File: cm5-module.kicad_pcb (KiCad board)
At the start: 4 copper layers, 100 x 100 mm, 156 parts, among them J1 DIN-41612-connector_090319679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, J10 MicroSD_5033981892, J2 CM5_1-100_3mm-stack, J3 CM5_101-200_3mm-stack, J4 JST_SH_1x3_BM03B-SRSS-TB-LF-SN, J5 Bus_M.2_1-2199230-6, J6 RJ45_HC612601A-M893-A, J7 USB-A_USB-303WSD-BRY, J8 HDMI-A_HDMI-19PIN-043, J9 USB-C_USB-310F-B-SU, Q1 SIS472DN-T1-GE3, Q2 SIS472DN-T1-GE3, Q3 AO3400A, U1 AP22615AWU-7, U10 AP22615AWU-7, U11 AP22615AWU-7, U2 AP22615AWU-7, U3 FT230XQ-R, U4 NTS0102DP, U5 CH334P, U6 LM74700QDBVRQ1, U7 SIC431AED-T1-GE3, U8 LM74700QDBVRQ1, U9 TPS564247DRLR, Y1 Oscillator_32.768kHz_OK2EL89C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, Y2 X322512MSB4SI

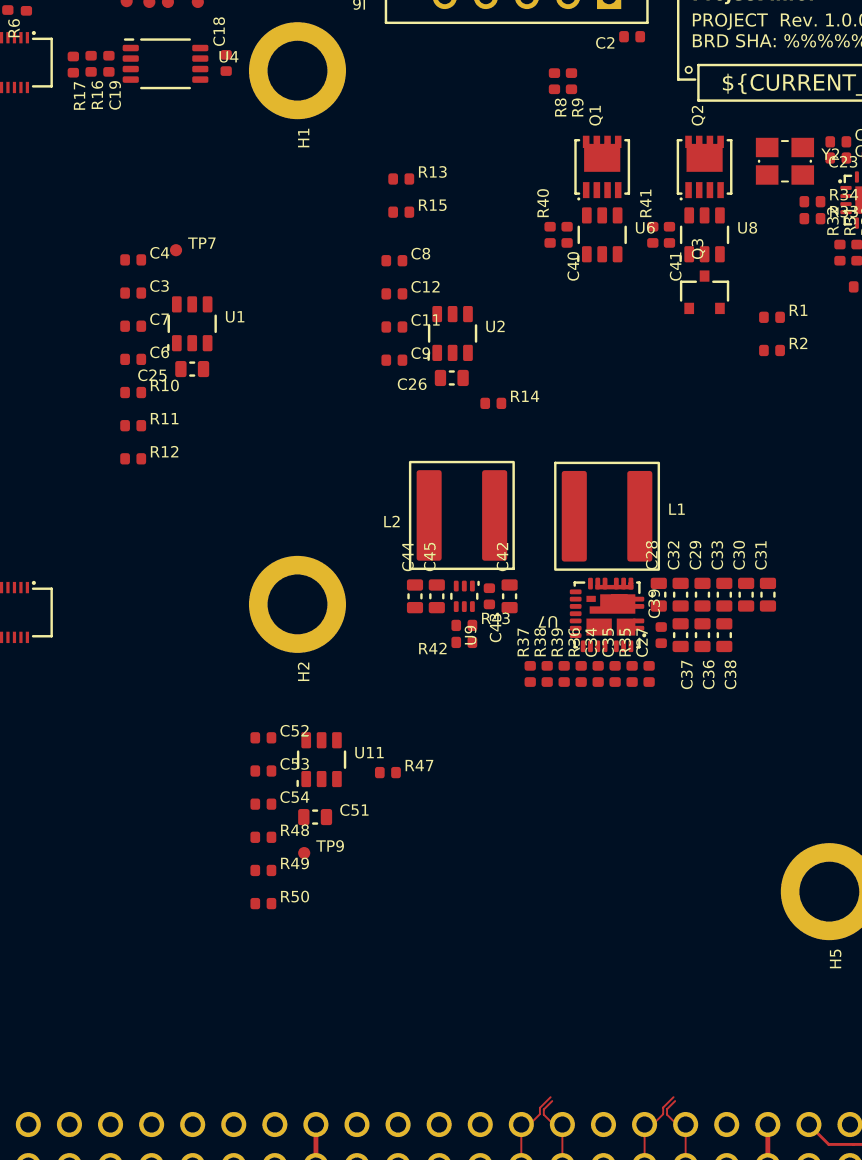
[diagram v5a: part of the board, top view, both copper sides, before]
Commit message: [#1] Finish schematic design of the 3V3 DC-DC converter
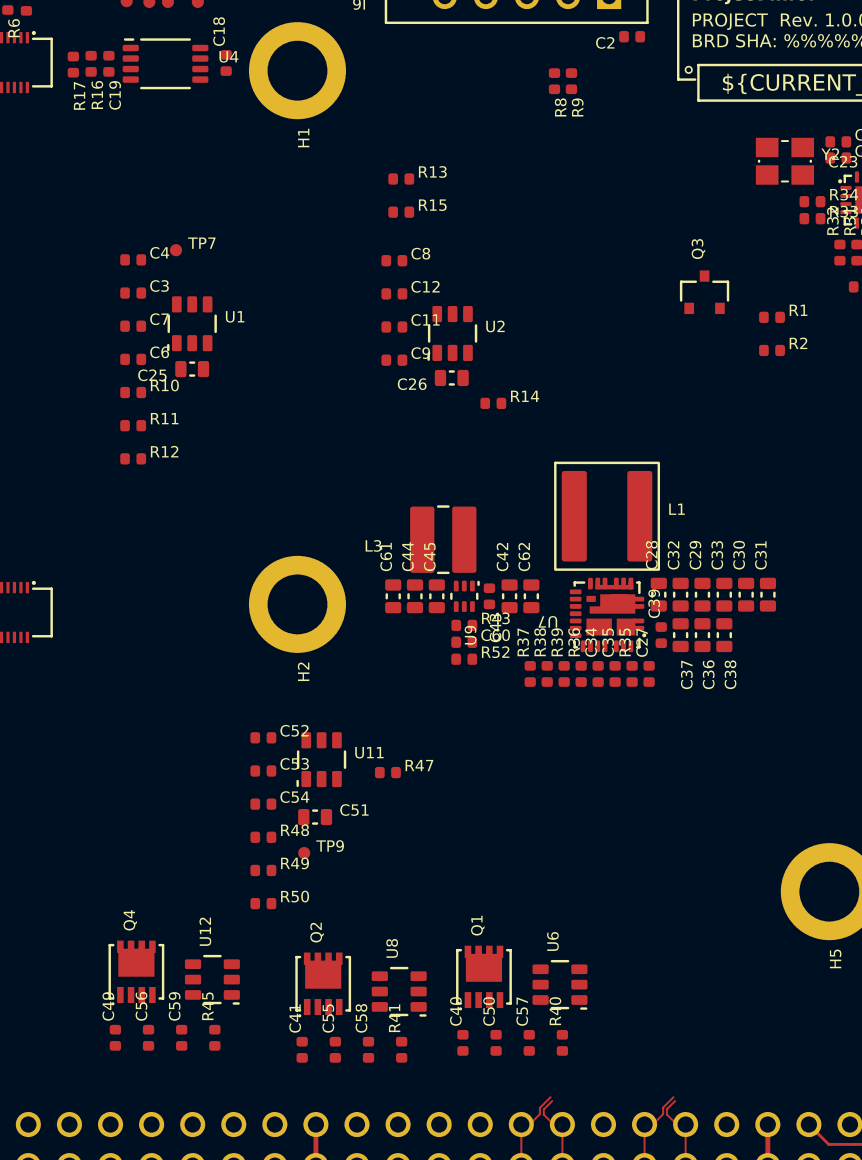
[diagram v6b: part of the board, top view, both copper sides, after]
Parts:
- removed L2: L-1u-20A-CJiang-FEXL0650A, DW-footprints:L-CJiang-FEXL0650A
- removed R42: R-10k-0402, DW-footprints:R_0402_1005Metric
- added C49: C-100n-0402, DW-footprints:C_0402_1005Metric, F.Cu at (83.3, 135.5)
- added C50: C-100n-0402, DW-footprints:C_0402_1005Metric, F.Cu at (106.9, 135.8)
- added C55: C-100n-0402, DW-footprints:C_0402_1005Metric, F.Cu at (96.9, 136.3)
- added C56: C-100n-0402, DW-footprints:C_0402_1005Metric, F.Cu at (85.4, 135.5)
- added C57: C-100n-0402, DW-footprints:C_0402_1005Metric, F.Cu at (108.9, 135.8)
- added C58: C-100n-0402, DW-footprints:C_0402_1005Metric, F.Cu at (99.0, 136.3)
- added C59: C-100n-0402, DW-footprints:C_0402_1005Metric, F.Cu at (87.4, 135.5)
- added C60: C-47p-0402, DW-footprints:C_0402_1005Metric, F.Cu at (104.9, 111.1)
- added C61: C-10u-0603, DW-footprints:C_0603_1608Metric, F.Cu at (100.5, 108.2)
- added C62: C-10u-0603, DW-footprints:C_0603_1608Metric, F.Cu at (109.0, 108.2)
- added L3: L-1u5-6.5A-CJiang-FTC404030S, DW-footprints:L-CJiang-FTC404030S, F.Cu at (103.6, 104.7)
- added Q4: SIS472DN-T1-GE3, DW-footprints:PowerPAK-1212-8_Single, F.Cu at (84.6, 131.5)
- added R45: R-10k-0402, DW-footprints:R_0402_1005Metric, F.Cu at (89.5, 135.5)
- added R52: R-45k3-0402, DW-footprints:R_0402_1005Metric, F.Cu at (104.9, 112.1)
- added U12: LM74700QDBVRQ1, DW-footprints:SOT-23-6, F.Cu at (89.3, 131.9)
- moved Q2 55.7 mm to (96.2, 132.2)
- moved C41 55.3 mm to (94.9, 136.3), turned to 90 degrees
- moved R41 52.7 mm to (101.0, 136.3)
- moved Q1 50.6 mm to (106.1, 131.8)
- moved U8 50.5 mm to (100.9, 132.7), turned to 90 degrees
- moved C40 50.4 mm to (104.8, 135.8), turned to 90 degrees
- moved R40 50.0 mm to (111.0, 135.8)
- moved U6 46.4 mm to (110.8, 132.2), turned to 90 degrees
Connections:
- net /Backplane/GPIOC0 renamed /Backplane/GPIO_C0
- net /Backplane/GPIOC1 renamed /Backplane/GPIO_C1
- net /Backplane/GPIOC10 renamed /Backplane/GPIO_C10
- net /Backplane/GPIOC11 renamed /Backplane/GPIO_C11
- net /Backplane/GPIOC12 renamed /Backplane/GPIO_C12
- net /Backplane/GPIOC13 renamed /Backplane/GPIO_C13
- net /Backplane/GPIOC14 renamed /Backplane/GPIO_C14
- net /Backplane/GPIOC15 renamed /Backplane/GPIO_C15
- net /Backplane/GPIOC2 renamed /Backplane/GPIO_C2
- net /Backplane/GPIOC3 renamed /Backplane/GPIO_C3
- net /Backplane/GPIOC4 renamed /Backplane/GPIO_C4
- net /Backplane/GPIOC5 renamed /Backplane/GPIO_C5
- net /Backplane/GPIOC6 renamed /Backplane/GPIO_C6
- net /Backplane/GPIOC7 renamed /Backplane/GPIO_C7
- net /Backplane/GPIOC8 renamed /Backplane/GPIO_C8
- net /Backplane/GPIOC9 renamed /Backplane/GPIO_C9
- net /Backplane/GPIOL0 renamed /Backplane/GPIO_L0
- net /Backplane/GPIOL1 renamed /Backplane/GPIO_L1
- net /Backplane/GPIOL10 renamed /Backplane/GPIO_L10
- net /Backplane/GPIOL11 renamed /Backplane/GPIO_L11
- net /Backplane/GPIOL12 renamed /Backplane/GPIO_L12
- net /Backplane/GPIOL13 renamed /Backplane/GPIO_L13
- net /Backplane/GPIOL14 renamed /Backplane/GPIO_L14
- net /Backplane/GPIOL15 renamed /Backplane/GPIO_L15
- net /Backplane/GPIOL2 renamed /Backplane/GPIO_L2
- net /Backplane/GPIOL3 renamed /Backplane/GPIO_L3
- net /Backplane/GPIOL4 renamed /Backplane/GPIO_L4
- net /Backplane/GPIOL5 renamed /Backplane/GPIO_L5
- net /Backplane/GPIOL6 renamed /Backplane/GPIO_L6
- net /Backplane/GPIOL7 renamed /Backplane/GPIO_L7
- net /Backplane/GPIOL8 renamed /Backplane/GPIO_L8
- net /Backplane/GPIOL9 renamed /Backplane/GPIO_L9
- net /Backplane/GPIOR0 renamed /Backplane/GPIO_R0
- net /Backplane/GPIOR1 renamed /Backplane/GPIO_R1
- net /Backplane/GPIOR10 renamed /Backplane/GPIO_R10
- net /Backplane/GPIOR11 renamed /Backplane/GPIO_R11
- net /Backplane/GPIOR12 renamed /Backplane/GPIO_R12
- net /Backplane/GPIOR13 renamed /Backplane/GPIO_R13
- net /Backplane/GPIOR14 renamed /Backplane/GPIO_R14
- net /Backplane/GPIOR15 renamed /Backplane/GPIO_R15
- net /Backplane/GPIOR2 renamed /Backplane/GPIO_R2
- net /Backplane/GPIOR3 renamed /Backplane/GPIO_R3
- net /Backplane/GPIOR4 renamed /Backplane/GPIO_R4
- net /Backplane/GPIOR5 renamed /Backplane/GPIO_R5
- net /Backplane/GPIOR6 renamed /Backplane/GPIO_R6
- net /Backplane/GPIOR7 renamed /Backplane/GPIO_R7
- net /Backplane/GPIOR8 renamed /Backplane/GPIO_R8
- net /Backplane/GPIOR9 renamed /Backplane/GPIO_R9
- net /USB hub/USB_1.D+ renamed /CAN to USB/USB.D+
- net /USB hub/USB_1.D- renamed /CAN to USB/USB.D-
- net /USB hub/USB_2.D+ renamed /CAN to USB1/USB.D+
- net /USB hub/USB_2.D- renamed /CAN to USB1/USB.D-
- net Net-(U6-EN) renamed /Power/Ideal diode 0/~{DISABLE}
- C15 pad 2: /USB console/+VBUS -> /Power/5V_USB_IN
- C16 pad 2: /USB console/+VBUS -> /Power/5V_USB_IN
- C40 pad 1: /Power/5V -> +5V_STDBY
- C41 pad 1: /Power/5V_USB_IN -> /Power/5V
- D3 pad 1: /USB console/+VBUS -> /Power/5V_USB_IN
- D4 pad 1: /USB console/CC2 -> /CM5/CC2
- D4 pad 10: /USB console/CC2 -> /CM5/CC2
- D4 pad 5: /USB console/CC1 -> /CM5/CC1
- D4 pad 6: /USB console/CC1 -> /CM5/CC1
- J2 pad 94: unconnected-(J2-CC1-Pad94) -> /CM5/CC1
- J2 pad 96: unconnected-(J2-CC2-Pad96) -> /CM5/CC2
- J9 pad A4: /USB console/+VBUS -> /Power/5V_USB_IN
- J9 pad A5: /USB console/CC1 -> /CM5/CC1
- J9 pad A9: /USB console/+VBUS -> /Power/5V_USB_IN
- J9 pad B4: /USB console/+VBUS -> /Power/5V_USB_IN
- J9 pad B5: /USB console/CC2 -> /CM5/CC2
- J9 pad B9: /USB console/+VBUS -> /Power/5V_USB_IN
- Q1 pad 1: /Power/5V -> +5V_STDBY
- Q1 pad 2: /Power/5V -> +5V_STDBY
- Q1 pad 3: /Power/5V -> +5V_STDBY
- Q2 pad 1: /Power/5V_USB_IN -> /Power/5V
- Q2 pad 2: /Power/5V_USB_IN -> /Power/5V
- Q2 pad 3: /Power/5V_USB_IN -> /Power/5V
- Q3 pad 3: Net-(Q3-D) -> /Power/Ideal diode 2/~{DISABLE}
- R22 pad 2: /USB console/+VBUS -> /Power/5V_USB_IN
- R24 pad 2: /USB console/CC2 -> /CM5/CC2
- R25 pad 2: /USB console/CC1 -> /CM5/CC1
- R3 pad 1: /CM5/CONSOLE.RX -> /CM5/UART2_TX
- R3 pad 2: /CM5/UART2_TX -> /CM5/CONSOLE.RX
- R4 pad 1: /CM5/CONSOLE.TX -> /CM5/UART2_RX
- R4 pad 2: /CM5/UART2_RX -> /CM5/CONSOLE.TX
- R40 pad 2: /Power/5V -> +5V_STDBY
- R41 pad 1: Net-(Q3-D) -> /Power/Ideal diode 1/~{DISABLE}
- R41 pad 2: /Power/5V_USB_IN -> /Power/5V
- U3 pad 10: /USB console/+VBUS -> /Power/5V_USB_IN
- U6 pad 6: /Power/5V -> +5V_STDBY
- U8 pad 3: Net-(Q3-D) -> /Power/Ideal diode 1/~{DISABLE}
- U8 pad 6: /Power/5V_USB_IN -> /Power/5V

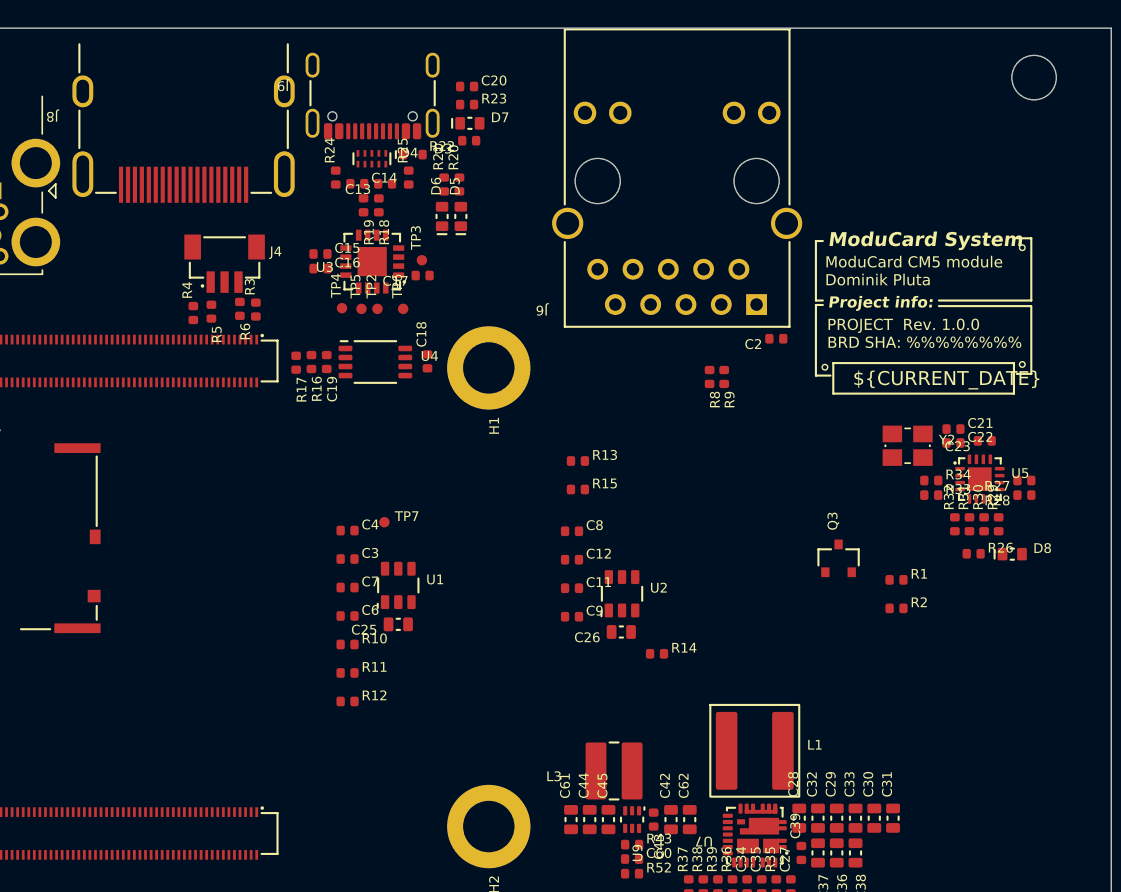
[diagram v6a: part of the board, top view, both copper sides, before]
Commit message: [#1] Add cooling fan connector
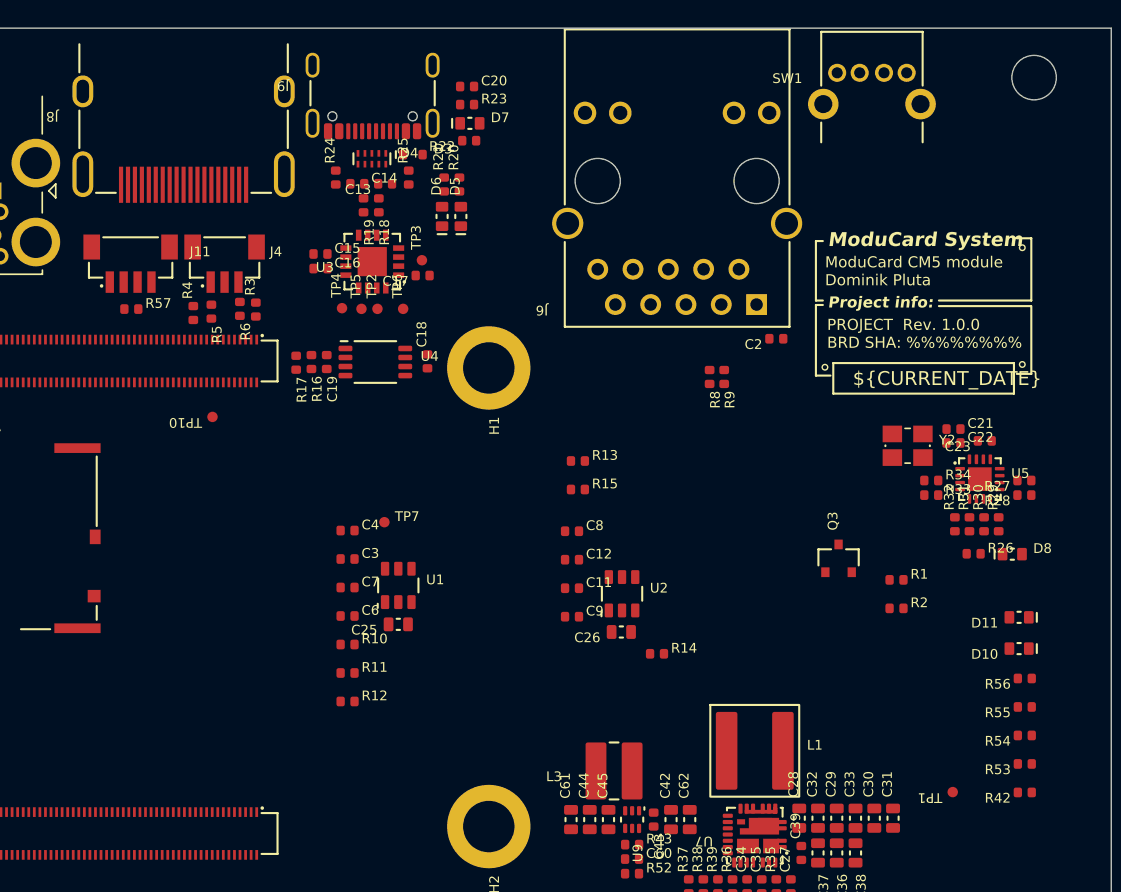
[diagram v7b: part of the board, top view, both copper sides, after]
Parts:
- added D10: LED-R-0603_KT-0603R, DW-footprints:LED_0603_1608Metric_R, F.Cu at (132.7, 95.9)
- added D11: LED-R-0603_KT-0603R, DW-footprints:LED_0603_1608Metric_R, F.Cu at (132.7, 93.7)
- added J11: JST_SH_1x4_BM04B-SRSS-TB-LF-SN, DW-footprints:Conn_JST_SH_1x4_BM04B-SRSS-TB, F.Cu at (68.8, 67.8)
- added R42: R-0R-0402, DW-footprints:R_0402_1005Metric, F.Cu at (133.2, 106.3)
- added R53: R-0R-0402, DW-footprints:R_0402_1005Metric, F.Cu at (133.2, 104.2)
- added R54: R-0R-0402, DW-footprints:R_0402_1005Metric, F.Cu at (133.2, 102.2)
- added R55: R-1k-0402, DW-footprints:R_0402_1005Metric, F.Cu at (133.2, 100.1)
- added R56: R-1k-0402, DW-footprints:R_0402_1005Metric, F.Cu at (133.2, 98.1)
- added R57: R-10k-0402, DW-footprints:R_0402_1005Metric, F.Cu at (68.9, 71.5)
- added SW1: SW_TL2243, DW-footprints:SW_TL2243, F.Cu at (124.7, 54.5)
- added TP1: TP_SMD_0.75mm, DW-footprints:TP_SMD_0.75mm, F.Cu at (128.0, 106.3)
- added TP10: TP_SMD_0.75mm, DW-footprints:TP_SMD_0.75mm, F.Cu at (74.7, 79.3)
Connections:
- J2 pad 16: unconnected-(J2-FAN_TACHO-Pad16) -> /CM5/FAN_TACHO
- J2 pad 18: unconnected-(J2-Ethernet_SYNC_OUT(3.3v)-Pad18) -> Net-(J2-Ethernet_SYNC_OUT)
- J2 pad 19: unconnected-(J2-FAN_PWM-Pad19) -> /CM5/FAN_PWM
- J2 pad 20: unconnected-(J2-EEPROM_nWP-Pad20) -> /CM5/~{EEPROM_WP}
- J2 pad 21: unconnected-(J2-LED_nACT-Pad21) -> /CM5/~{LED_ACT}
- J2 pad 35: unconnected-(J2-ID_SC-Pad35) -> /CM5/SCL1
- J2 pad 36: unconnected-(J2-ID_SD-Pad36) -> /CM5/SDA1
- J2 pad 77: +5v_(Input) -> +5V
- J2 pad 79: +5v_(Input) -> +5V
- J2 pad 80: unconnected-(J2-SCL0-Pad80) -> /CM5/SCL0
- J2 pad 81: +5v_(Input) -> +5V
- J2 pad 82: unconnected-(J2-SDA0-Pad82) -> /CM5/SDA0
- J2 pad 83: +5v_(Input) -> +5V
- J2 pad 85: +5v_(Input) -> +5V
- J2 pad 87: +5v_(Input) -> +5V
- J2 pad 89: unconnected-(J2-WiFi_nDisable-Pad89) -> /CM5/~{WiFi_DIS}
- J2 pad 91: unconnected-(J2-BT_nDisable-Pad91) -> /CM5/~{BT_DIS}
- J2 pad 92: unconnected-(J2-PWR_BUT-Pad92) -> /CM5/PWR_BTN
- J2 pad 93: unconnected-(J2-nRPIBOOT-Pad93) -> /CM5/~{RPIBOOT}
- J2 pad 95: unconnected-(J2-LED_nPWR-Pad95) -> /CM5/~{LED_PWR}
- J2 pad 99: unconnected-(J2-PMIC_ENABLE-Pad99) -> /CM5/PMIC_EN
